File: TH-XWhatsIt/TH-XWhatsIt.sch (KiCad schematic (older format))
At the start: 36 parts, among them J1 COLUMNS, J12 EXPANSION HEADER, J13 Conn_01x02, J2 ROWS, U1 LM339, U2 MCP4921-EP, U3 74HCT595, U5 74HCT595, U6 LM339, U7 ProMicro, U8 74HCT595

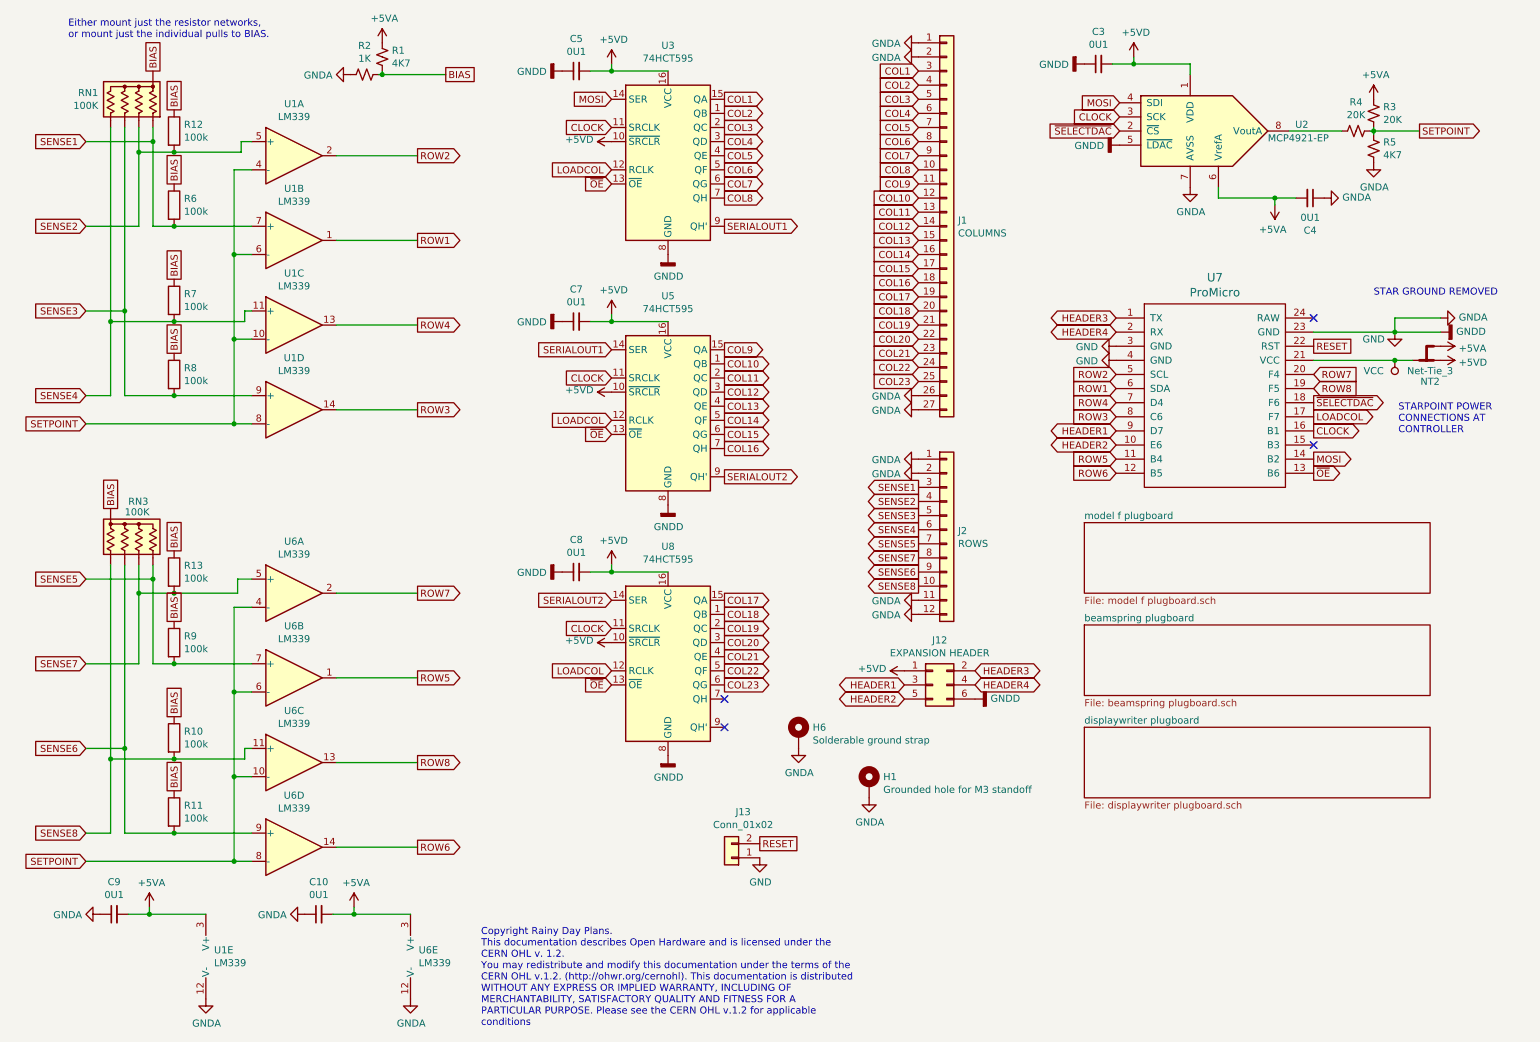
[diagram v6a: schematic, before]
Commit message: Added locklights header, bumped revision
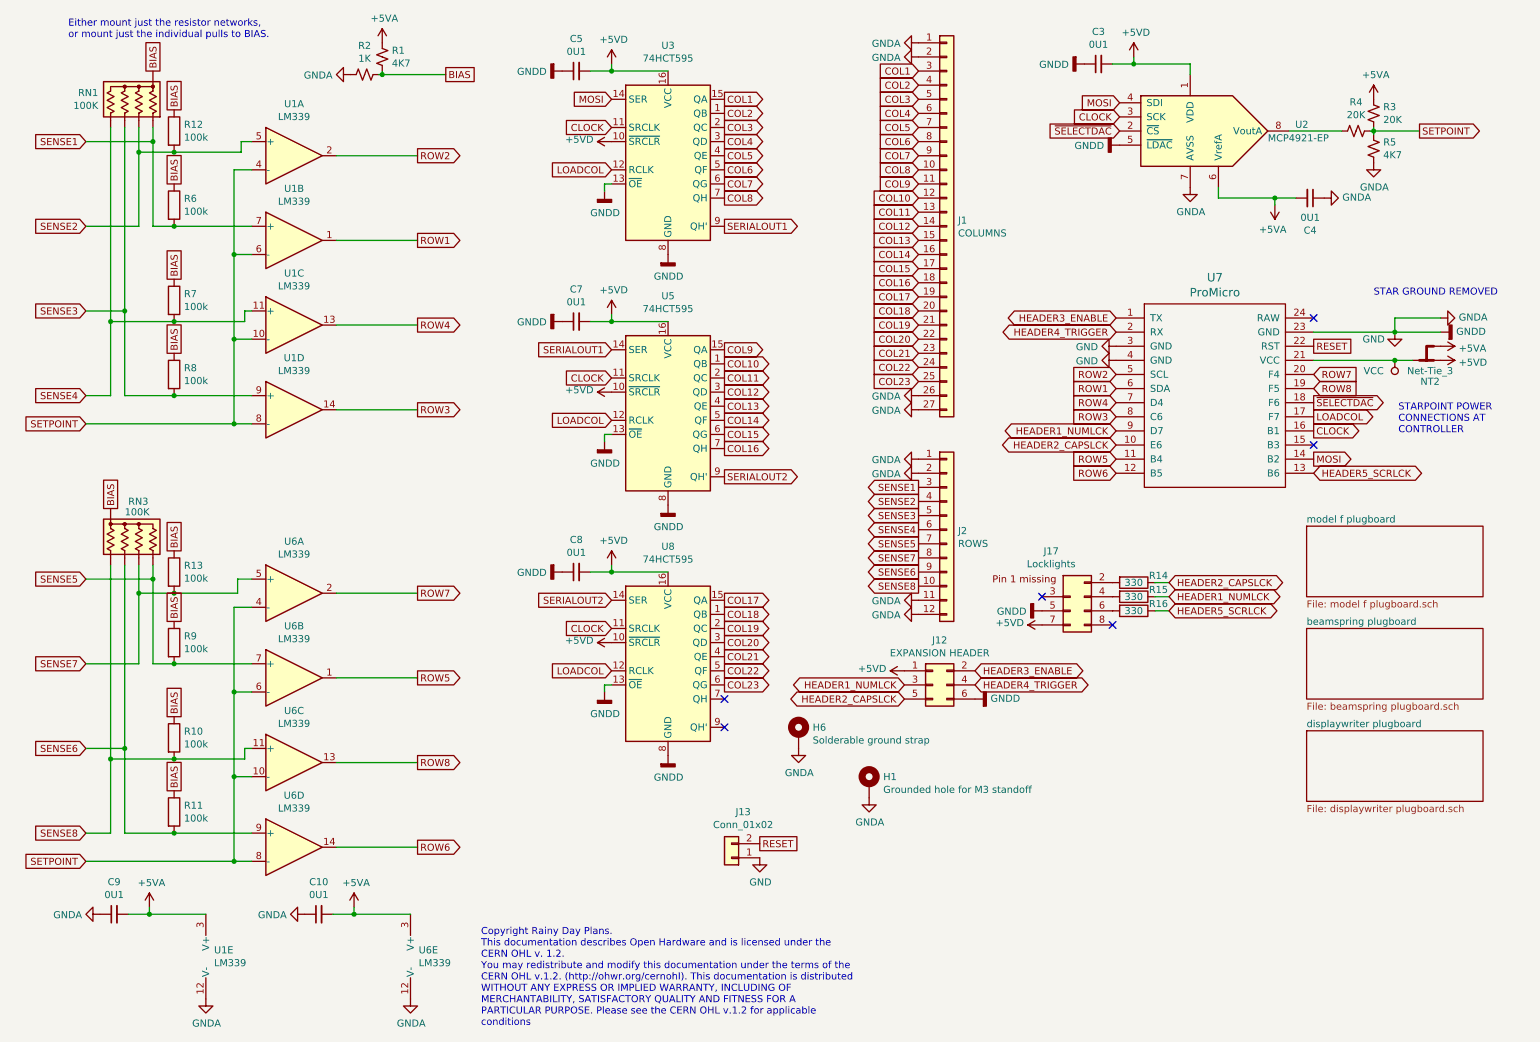
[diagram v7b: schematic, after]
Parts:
- added J17: Locklights, TH-XWhatsIt:FAT_LockLightsConnector, symbol fatlocklights:Conn_02x04_Odd_Even
- added R14, R15, R16: 330, Resistor_THT:R_Axial_DIN0204_L3.6mm_D1.6mm_P7.62mm_Horizontal, symbol Device:R
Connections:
- net +5VD: now also J17.7 (Pin_7)
- net GND: now also U3.13 (~OE), U5.13 (~OE), U8.13 (~OE), J17.5 (Pin_5)
- net HEADER1 renamed HEADER1_NUMLCK
- net HEADER1_NUMLCK: now also R15.1
- net HEADER2 renamed HEADER2_CAPSLCK
- net HEADER2_CAPSLCK: now also R14.1
- net HEADER3 renamed HEADER3_ENABLE
- net HEADER4 renamed HEADER4_TRIGGER
- removed net ~OE: U3.13 (~OE), U5.13 (~OE), U7.13 (B6), U8.13 (~OE)
- new net: J17.2 (Pin_2), R14.2
- new net: J17.4 (Pin_4), R15.2
- new net: J17.6 (Pin_6), R16.2
- new net HEADER5_SCRLCK: R16.1, U7.13 (B6)
- no-connect marks 4 -> 6
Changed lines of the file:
@@
 Title "TH-XWhatsIt combined beamspring and model f controller"
 Date "2020-01-31"
-Rev "0.1.2"
+Rev "0.1.3"
 Comp "Rainy Day Plans"
 Comment1 ""
@@
 Text GLabel 4875 1375 0    50   Input ~ 0
 CLOCK
-Text GLabel 4875 1775 0    50   Input ~ 0
-~OE
 $Comp
 L Device:R_Network04_US RN3
@@
 Wire Wire Line
 	4875 2700 4875 2750
-Text GLabel 4875 3550 0    50   Input ~ 0
-~OE
 $Comp
 L 74xx:74HCT595 U8
@@
 Wire Wire Line
 	4875 4475 4875 4525
-Text GLabel 4875 5325 0    50   Input ~ 0
-~OE
 Text GLabel 5675 2075 2    50   Output ~ 0
 SERIALOUT1
@@
 Text GLabel 9850 3425 2    50   Output ~ 0
 LOADCOL
-Text GLabel 9850 3825 2    50   Output ~ 0
-~OE
 $Comp
 L Connector_Generic:Conn_01x27 J1
@@
 $EndComp
 $Sheet
-S 8225 4175 2450 500
-U 5E97697F
-F0 "model f plugboard" 50
-F1 "model f plugboard.sch" 50
-$EndSheet
-$Sheet
-S 8225 4900 2450 500
+S 9800 4925 1250 500
 U 5E9772A5
 F0 "beamspring plugboard" 50
 F1 "beamspring plugboard.sch" 50
-$EndSheet
-$Sheet
-S 8225 5625 2450 500
-U 5E995B14
-F0 "displaywriter plugboard" 50
-F1 "displaywriter plugboard.sch" 50
 $EndSheet
 Text GLabel 7050 3925 0    50   Output ~ 0
@@
 $EndComp
 Text GLabel 7450 5225 2    50   BiDi ~ 0
-HEADER3
+HEADER3_ENABLE
 Text GLabel 7450 5325 2    50   BiDi ~ 0
-HEADER4
+HEADER4_TRIGGER
 Text GLabel 8450 3525 0    50   BiDi ~ 0
-HEADER1
+HEADER1_NUMLCK
 Text GLabel 8450 3625 0    50   BiDi ~ 0
-HEADER2
+HEADER2_CAPSLCK
 Text GLabel 8450 2725 0    50   BiDi ~ 0
-HEADER3
+HEADER3_ENABLE
 Text GLabel 8450 2825 0    50   BiDi ~ 0
-HEADER4
+HEADER4_TRIGGER
 Text GLabel 6950 5425 0    50   BiDi ~ 0
-HEADER2
+HEADER2_CAPSLCK
 Text GLabel 6950 5325 0    50   BiDi ~ 0
-HEADER1
+HEADER1_NUMLCK
 Text Notes 3950 7750 0    50   ~ 0
 Copyright Rainy Day Plans.\nThis documentation describes Open Hardware and is licensed under the\nCERN OHL v. 1.2.\nYou may redistribute and modify this documentation under the terms of the\nCERN OHL v.1.2. (http://ohwr.org/cernohl). This documentation is distributed\nWITHOUT ANY EXPRESS OR IMPLIED WARRANTY, INCLUDING OF\nMERCHANTABILITY, SATISFACTORY QUALITY AND FITNESS FOR A\nPARTICULAR PURPOSE. Please see the CERN OHL v.1.2 for applicable\nconditions
@@
 	1    0    0    -1
 $EndComp
+$Comp
+L power:GNDD #PWR01
+U 1 1 5FCF2103
+P 4825 1825
+F 0 "#PWR01" H 4825 1575 50  0001 C CNN
+F 1 "GNDD" H 4829 1670 50  0000 C CNN
+F 2 "" H 4825 1825 50  0001 C CNN
+F 3 "" H 4825 1825 50  0001 C CNN
+	1    4825 1825
+	1    0    0    -1
+$EndComp
+$Comp
+L power:GNDD #PWR02
+U 1 1 5FCF2E36
+P 4825 3600
+F 0 "#PWR02" H 4825 3350 50  0001 C CNN
+F 1 "GNDD" H 4829 3445 50  0000 C CNN
+F 2 "" H 4825 3600 50  0001 C CNN
+F 3 "" H 4825 3600 50  0001 C CNN
+	1    4825 3600
+	1    0    0    -1
+$EndComp
+$Comp
+L power:GNDD #PWR03
+U 1 1 5FCF5D69
+P 4825 5375
+F 0 "#PWR03" H 4825 5125 50  0001 C CNN
+F 1 "GNDD" H 4829 5220 50  0000 C CNN
+F 2 "" H 4825 5375 50  0001 C CNN
+F 3 "" H 4825 5375 50  0001 C CNN
+	1    4825 5375
+	1    0    0    -1
+$EndComp
+Wire Wire Line
+	4825 5375 4825 5325
+Wire Wire Line
+	4825 5325 4875 5325
+Wire Wire Line
+	4825 3600 4825 3550
+Wire Wire Line
+	4825 3550 4875 3550
+Wire Wire Line
+	4825 1825 4825 1775
+Wire Wire Line
+	4825 1775 4875 1775
+$Sheet
+S 9800 4200 1250 500
+U 5E97697F
+F0 "model f plugboard" 50
+F1 "model f plugboard.sch" 50
+$EndSheet
+$Sheet
+S 9800 5650 1250 500
+U 5E995B14
+F0 "displaywriter plugboard" 50
+F1 "displaywriter plugboard.sch" 50
+$EndSheet
+Text GLabel 9850 3825 2    50   BiDi ~ 0
+HEADER5_SCRLCK
+$Comp
+L fatlocklights:Conn_02x04_Odd_Even J17
+U 1 1 5FD7300D
+P 8125 4700
+F 0 "J17" H 7990 5023 50  0000 C CNN
+F 1 "Locklights" H 7990 4932 50  0000 C CNN
+F 2 "TH-XWhatsIt:FAT_LockLightsConnector" H 8125 4700 50  0001 C CNN
+F 3 "~" H 8125 4700 50  0001 C CNN
+	1    8125 4700
+	1    0    0    -1
+$EndComp
+$Comp
+L power:GNDD #PWR04
+U 1 1 5FD74441
+P 7925 4800
+F 0 "#PWR04" H 7925 4550 50  0001 C CNN
+F 1 "GNDD" V 7929 4690 50  0000 R CNN
+F 2 "" H 7925 4800 50  0001 C CNN
+F 3 "" H 7925 4800 50  0001 C CNN
+	1    7925 4800
+	0    1    1    0
+$EndComp
+NoConn ~ 7925 4700
+$Comp
+L power:+5VD #PWR05
+U 1 1 5FD7927F
+P 7925 4900
+F 0 "#PWR05" H 7925 4750 50  0001 C CNN
+F 1 "+5VD" V 7940 5028 50  0000 L CNN
+F 2 "" H 7925 4900 50  0001 C CNN
+F 3 "" H 7925 4900 50  0001 C CNN
+	1    7925 4900
+	0    -1   -1   0
+$EndComp
+$Comp
+L Device:R R14
+U 1 1 5FD7A089
+P 8575 4600
+F 0 "R14" V 8525 4775 50  0000 C CNN
+F 1 "330" V 8575 4600 50  0000 C CNN
+F 2 "Resistor_THT:R_Axial_DIN0204_L3.6mm_D1.6mm_P7.62mm_Horizontal" V 8505 4600 50  0001 C CNN
+F 3 "~" H 8575 4600 50  0001 C CNN
+	1    8575 4600
+	0    1    1    0
+$EndComp
+$Comp
+L Device:R R15
+U 1 1 5FD7C563
+P 8575 4700
+F 0 "R15" V 8525 4875 50  0000 C CNN
+F 1 "330" V 8575 4700 50  0000 C CNN
+F 2 "Resistor_THT:R_Axial_DIN0204_L3.6mm_D1.6mm_P7.62mm_Horizontal" V 8505 4700 50  0001 C CNN
+F 3 "~" H 8575 4700 50  0001 C CNN
+	1    8575 4700
+	0    1    1    0
+$EndComp
+$Comp
+L Device:R R16
+U 1 1 5FD7E99A
+P 8575 4800
+F 0 "R16" V 8525 4975 50  0000 C CNN
+F 1 "330" V 8575 4800 50  0000 C CNN
+F 2 "Resistor_THT:R_Axial_DIN0204_L3.6mm_D1.6mm_P7.62mm_Horizontal" V 8505 4800 50  0001 C CNN
+F 3 "~" H 8575 4800 50  0001 C CNN
+	1    8575 4800
+	0    1    1    0
+$EndComp
+NoConn ~ 8425 4900
+Text GLabel 8825 4600 2    50   BiDi ~ 0
+HEADER2_CAPSLCK
+Text GLabel 8825 4700 2    50   BiDi ~ 0
+HEADER1_NUMLCK
+Text GLabel 8825 4800 2    50   BiDi ~ 0
+HEADER5_SCRLCK
+Wire Wire Line
+	8725 4600 8825 4600
+Wire Wire Line
+	8825 4700 8725 4700
+Wire Wire Line
+	8725 4800 8825 4800
 $EndSCHEMATC
